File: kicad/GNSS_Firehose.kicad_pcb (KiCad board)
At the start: 4 copper layers, 117.9 x 99.1 mm, 4 parts

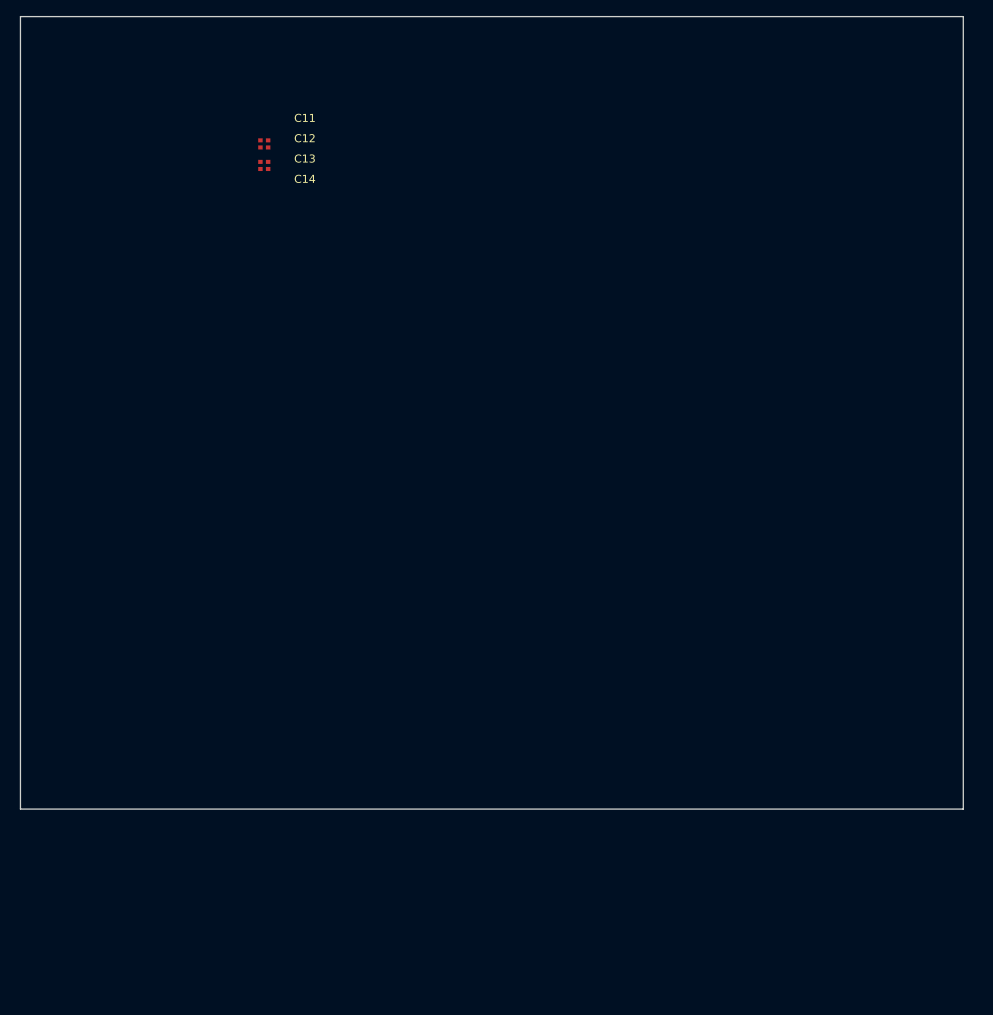
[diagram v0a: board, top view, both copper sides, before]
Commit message: footprints and footprint assignments
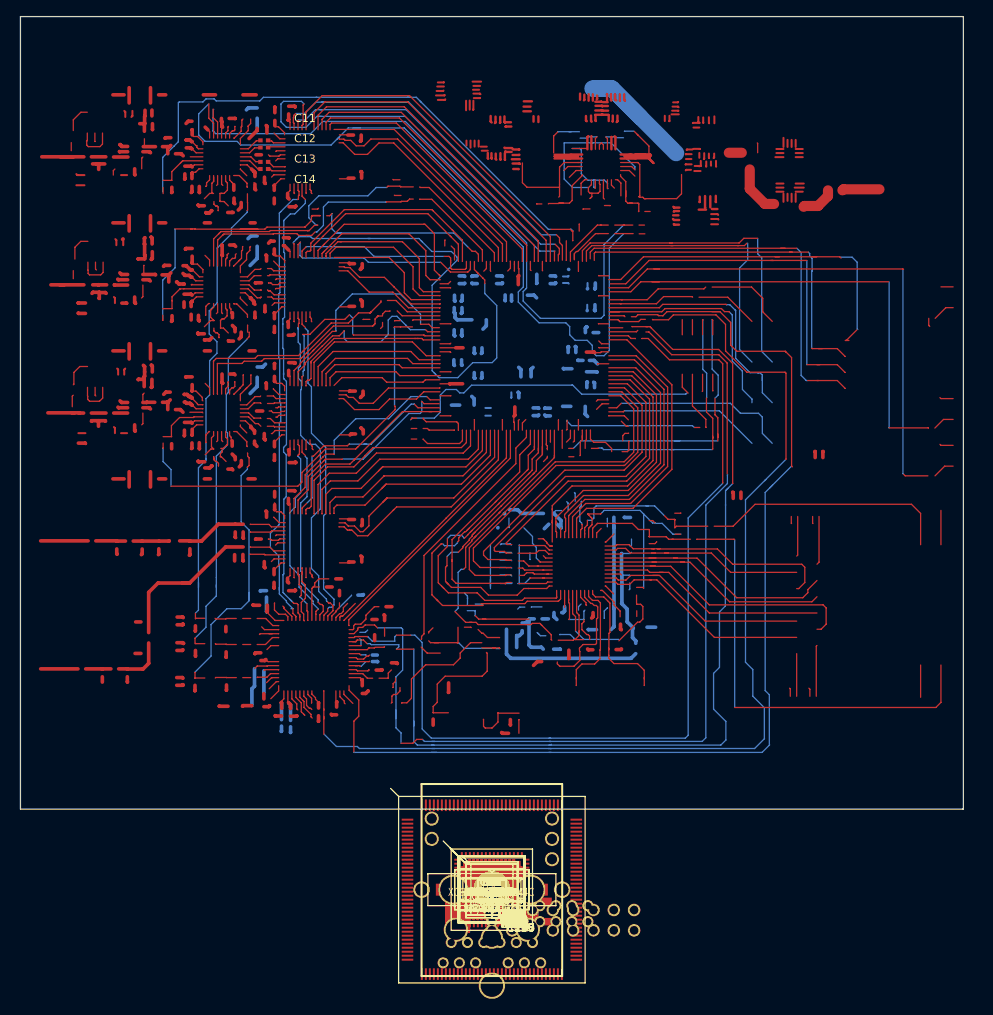
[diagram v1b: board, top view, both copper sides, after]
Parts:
- added C1, C10, C102, C108, C109, C110, C111, C112, C67, C73, C74, C75, C76, C77: 47 nF, footprints:0402, F.Cu at (132.6, 152.3)
- added C100, C116, C117, C126, C127, C128, C129, C130, C131, C132, C133, C134, C135, C137, C138, C139, C140, C141, C143, C144, C145, C146, C147, C149, C150, C151, C152, C153, C155, C156, C157, C159, C160, C161, C163, C164, C165, C167, C168, C18, C182, C183, C184, C185, C186, C187, C19, C201, C202, C203, C204, C205, C206, C207, C208, C209, C210, C211, C212, C218, C219, C221, C222, C223, C224, C227, C228, C229, C230, C248, C249, C250, C251, C252, C253, C254, C28, C29, C30, C31, C32, C33, C34, C35, C36, C37, C41, C42, C43, C44, C45, C46, C47, C49, C51, C54, C55, C56, C57, C58, C59, C60, C61, C62, C63, C64, C65, C66, C81, C82, C91, C92, C93, C94, C95, C96, C97, C98, C99: 0.1 uF, footprints:0402, F.Cu at (132.6, 152.3)
- added C103, C5, C68: 10 nF, footprints:0402, F.Cu at (132.6, 152.3)
- added C104, C105, C106, C107, C115, C125, C17, C27, C6, C69, C7, C70, C71, C72, C8, C80, C9, C90: 100 pF, footprints:0402, F.Cu at (132.6, 152.3)
- added C113, C15, C78: 2.2 nF, footprints:0402, F.Cu at (132.6, 152.3)
- added C114, C16, C79: 33 nF, footprints:0402, F.Cu at (132.6, 152.3)
- added C118, C119, C120, C121, C122, C123, C124, C20, C21, C22, C23, C24, C242, C243, C244, C245, C246, C247, C25, C26, C83, C84, C85, C86, C87, C88, C89: 1000 pF, footprints:0402, F.Cu at (132.6, 152.3)
- added C142, C148, C154, C158, C162, C166, C193, C216, C217, C220, C225, C226, C53: 10 uF, footprints:0805, F.Cu at (132.6, 152.3)
- added C176, C177: 33 pF, footprints:0402, F.Cu at (132.6, 152.3)
- added C194, C198: 47 uF 20V, footprints:tantalum-size-D, F.Cu at (132.6, 152.3)
- added C195: 2.2 uF, footprints:0603, F.Cu at (132.6, 152.3)
- added C196: 47 uF, footprints:1210, F.Cu at (132.6, 152.3)
- added C197, C199: 0.1 uF 25V, footprints:0402, F.Cu at (132.6, 152.3)
- added C200: 22 uF, footprints:1210, F.Cu at (132.6, 152.3)
- added C213, C237: NONE, footprints:1210, F.Cu at (132.6, 152.3)
- added C214: 220 pF, footprints:0402, F.Cu at (132.6, 152.3)
- added C215: 18 nF, footprints:0603, F.Cu at (132.6, 152.3)
- added C231, C232, C233, C234, C235, C236, C255: 10 pF, footprints:0402, F.Cu at (132.6, 152.3)
- added C238, C239, C240, C241, R108, R111, R112, R114, R115, R120, R121, R122, R125, R129, R130: NONE, footprints:0402, F.Cu at (132.6, 152.3)
- added FB1, FB11, FB12, FB13, FB14, FB15, FB16, FB2, FB3: 240, footprints:0603, F.Cu at (132.6, 152.3)
- added FB10, FB17, FB4, FB5, FB6, FB7, FB8, FB9: 240, footprints:0402, F.Cu at (132.6, 152.3)
- added FID1, FID2, FID3: fiducial, footprints:FIDUCIAL, F.Cu at (132.6, 152.3)
- added J1, J2, J3, J4, J5: SMA, footprints:SMA_END_LAUNCH, F.Cu at (132.6, 152.3)
- added J10: HEADER_16, footprints:HEADER16_100MIL, F.Cu at (132.6, 152.3)
- added J6: HEADER_14, footprints:HEADER14_2MM, F.Cu at (132.6, 152.3)
- added J7: L829-1J1T-43, footprints:L829-1J1T-43, F.Cu at (132.6, 152.3)
- added J8: PJ-063BH, footprints:PJ-063BH, F.Cu at (132.6, 152.3)
- added L10: 0.47 uF, footprints:NRS5020, F.Cu at (132.6, 152.3)
- added L11: 1 uH, footprints:NRS5020, F.Cu at (132.6, 152.3)
- added L12, L13, L14, L3, L5, L7: 47 nH, footprints:0402, F.Cu at (132.6, 152.3)
- added L15, L17, L19: 56 nH, footprints:0603, F.Cu at (132.6, 152.3)
- added L2, L4, L6: 6 nH, footprints:0402, F.Cu at (132.6, 152.3)
- added L20, L21, R126, R127, R128, R132, R98, R99: 0, footprints:0603, F.Cu at (132.6, 152.3)
- added LED1: LED, footprints:0603, F.Cu at (132.6, 152.3)
- added LED2, LED3, LED4: LED, footprints:APA2106, F.Cu at (132.6, 152.3)
- added MH1, MH2, MH3, MH4: mounting_hole, footprints:HOLE_UNC_2_56, F.Cu at (132.6, 152.3)
- added OSC1: TCXO, footprints:D75J, F.Cu at (132.6, 152.3)
- added Q1: Si2369DS, footprints:SOT23, F.Cu at (132.6, 152.3)
- added R1, R17, R25: 86.6, footprints:0402, F.Cu at (132.6, 152.3)
- added R10, R51, R52: 220, footprints:0402, F.Cu at (132.6, 152.3)
- added R100, R101, R102, R103, R104, R105: 33, footprints:0402, F.Cu at (132.6, 152.3)
- added R106, R109, R110, R113, R118, R119, R123, R137, R138, R139, R140, R141, R142, R40, R41, R86: 1k, footprints:0402, F.Cu at (132.6, 152.3)
- added R107, R44, R47: 4.7k, footprints:0402, F.Cu at (132.6, 152.3)
- added R11, R13, R15, R23, R31, R7: 80, footprints:0402, F.Cu at (132.6, 152.3)
- added R116, R117, R124, R146, R147, R148, R149, R150, R22, R30, R46, R6, R72, R73, R76, R77, R78, R79, R80, R81, R82, R83, R84, R97: 10k, footprints:0402, F.Cu at (132.6, 152.3)
- added R131, R135, R136, R42: 0, footprints:0402, F.Cu at (132.6, 152.3)
- added R133: 10, footprints:0603, F.Cu at (132.6, 152.3)
- added R143, R87: 0, footprints:1210, F.Cu at (132.6, 152.3)
- added R144: 10, footprints:0402, F.Cu at (132.6, 152.3)
- added R145: 0, footprints:0805, F.Cu at (132.6, 152.3)
- added R18, R2, R26: 5.1k, footprints:0402, F.Cu at (132.6, 152.3)
- added R19, R27, R3: 43.2, footprints:0402, F.Cu at (132.6, 152.3)
- added R20, R28, R4, R88: 820, footprints:0402, F.Cu at (132.6, 152.3)
- added R21, R29, R5: 390, footprints:0402, F.Cu at (132.6, 152.3)
- added R33, R37: 49.9, footprints:0402, F.Cu at (132.6, 152.3)
- added R34, R35: 60.4, footprints:0402, F.Cu at (132.6, 152.3)
- added R36: 249, footprints:0402, F.Cu at (132.6, 152.3)
- added R38, R39, R43, R48: 47, footprints:0402, F.Cu at (132.6, 152.3)
- added R45, R49, R50, R75, R85: 330, footprints:0402, F.Cu at (132.6, 152.3)
- added R70: 54.9k, footprints:0402, F.Cu at (132.6, 152.3)
- added R71: 12.1k, footprints:0402, F.Cu at (132.6, 152.3)
- added R74: 162k, footprints:0402, F.Cu at (132.6, 152.3)
- added R9: 150, footprints:0402, F.Cu at (132.6, 152.3)
- added R95: 12.1k 1%, footprints:0402, F.Cu at (132.6, 152.3)
- added R96: 470, footprints:0402, F.Cu at (132.6, 152.3)
- added SC1, SC2, SC3, SC4, SC5, SC6, SC7, SC8: shield_clip, footprints:S1721, F.Cu at (132.6, 152.3)
- added TP1, TP10, TP11, TP12, TP13, TP14, TP15, TP16, TP17, TP18, TP19, TP2, TP20, TP22, TP23, TP24, TP25, TP26, TP27, TP28, TP29, TP3, TP4, TP5, TP6, TP7, TP8, TP9: test_point, footprints:TP_SMT, F.Cu at (132.6, 152.3)
- added U1, U4, U7: MAX2112, footprints:QFN28_EP, F.Cu at (132.6, 152.3)
- added U10, U2, U5, U8: MAX19505, footprints:QFN48_EP, F.Cu at (132.6, 152.3)
- added U11: AT25DF041A, footprints:SO8, F.Cu at (132.6, 152.3)
- added U12: XC6SLX9-2TQG144C, footprints:LQFP144, F.Cu at (132.6, 152.3)
- added U15: LMK03806, footprints:LLP64_EP, F.Cu at (132.6, 152.3)
- added U17: LTC3633, footprints:UFD28, F.Cu at (132.6, 152.3)
- added U18: KSZ9031RNX, footprints:QFN48_EP_MICREL, F.Cu at (132.6, 152.3)
- added U19: CDCLVC1102, footprints:TSSOP8W, F.Cu at (132.6, 152.3)
- added U20, U21, U22: MIC2090-1YM5, footprints:SOT-23-5, F.Cu at (132.6, 152.3)
- added U3, U6, U9: MGA-68563, footprints:SOT-363, F.Cu at (132.6, 152.3)
- added Y1: 25 MHz, footprints:CTS_ATS, F.Cu at (132.6, 152.3)
- added Z1: SMAJ9.0CA, footprints:SMAJ, F.Cu at (132.6, 152.3)
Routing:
- net (no net): track 0.00 -> 6403.4 mm
- net Net-(C11-Pad1): track 0.00 -> 3.02 mm
- net Net-(C14-Pad1): track 0.00 -> 3.02 mm
- net Net-(C12-Pad1): track 0.00 -> 2.86 mm
- net Net-(C13-Pad1): track 0.00 -> 2.86 mm
- net Net-(C13-Pad2): track 0.00 -> 2.66 mm
- net Net-(C11-Pad2): track 0.00 -> 2.31 mm
- net Net-(C14-Pad2): track 0.00 -> 2.29 mm
- net Net-(C12-Pad2): track 0.00 -> 2.24 mm

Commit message: initial placement and wires
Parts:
- C141, C142, C143, C144, C145, C146, C147, C148, C149, C150, C151, C152, C153, C154, C155, C156, C157, C158, C159, C160, C161, C162, C163, C164, C165, C166, C167, C168, C182, C183, C184, C185, C186, C187, C193, C197, C199, C216, C217, C218, C219, C222, C223, C224, C225, C226, C227, C228, C59, C63, C65, FB1, FB11, FB12, FB13, FB3, FB4, FB5, FB7, FB9, R106, R107, R112, R113, R114, R115, R116, R117, R118, R119, R120, R121, R122, R123, R98, R99: moved to B.Cu
- moved FID3 117.2 mm to (76.2, 49.5)
- moved MH1 112.9 mm to (81.9, 51.4)
- moved MH2 112.9 mm to (183.3, 51.4)
- moved J1 109.1 mm to (73.2, 60.8), turned to 90 degrees
- moved SC1 108.7 mm to (88.5, 53.0)
- moved R126 107.8 mm to (80.1, 58.2), turned to 90 degrees
- moved U20 107.3 mm to (82.0, 57.7)
- moved C243 106.7 mm to (87.1, 55.7)
- moved J8 106.3 mm to (192.9, 64.8), turned to 270 degrees
- moved L12 106.1 mm to (80.0, 60.2), turned to 270 degrees
- moved C5 105.8 mm to (89.7, 55.6)
- moved C7 104.9 mm to (89.7, 56.6)
- moved C6 104.6 mm to (82.0, 60.7)
- moved SC2 104.6 mm to (99.8, 53.0)
- moved L3 103.9 mm to (89.2, 58.0), turned to 270 degrees
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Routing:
- net (no net): track 6403.4 -> 2297.0 mm
- net GND: track 0.00 -> 357.5 mm, vias 0 -> 1
- net VCC_3.3V: track 0.00 -> 235.2 mm
- net /Ethernet/DVDDL: track 0.00 -> 50.6 mm
- net PHY_RXD3: track 0.00 -> 46.7 mm
- net CH1_CLK: track 0.00 -> 44.0 mm
- net PHY_RX_CTL: track 0.00 -> 43.0 mm
- net PHY_RXD0: track 0.00 -> 42.3 mm
- net CH1_D7: track 0.00 -> 41.5 mm
- net PHY_RXD1: track 0.00 -> 40.1 mm
- net CH1_D6: track 0.00 -> 39.3 mm
- net VCC_1.2V: track 0.00 -> 38.7 mm
- net PHY_RXD2: track 0.00 -> 38.6 mm
- net CH1_D5: track 0.00 -> 37.1 mm
- net Net-(TP22-Pad1): track 0.00 -> 36.7 mm
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- added copper zone on In1.Cu, net GND
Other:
- net class Default: clearance 0.2 -> 0.1524; trace_width 0.25 -> 0.1524; via_dia 0.6 -> 0.6096; via_drill 0.4 -> 0.3048
- net class wide added: clearance 0.1524, trace_width 0.4572, via_dia 0.6096, via_drill 0.3048
- rule pad_to_mask_clearance: 0.2 -> 0
- rule trace_clearance: 0.2 -> 0.1524
- rule trace_min: 0.2 -> 0.1524
- rule via_min_drill: 0.3 -> 0.3048
- rule via_min_size: 0.4 -> 0.6096

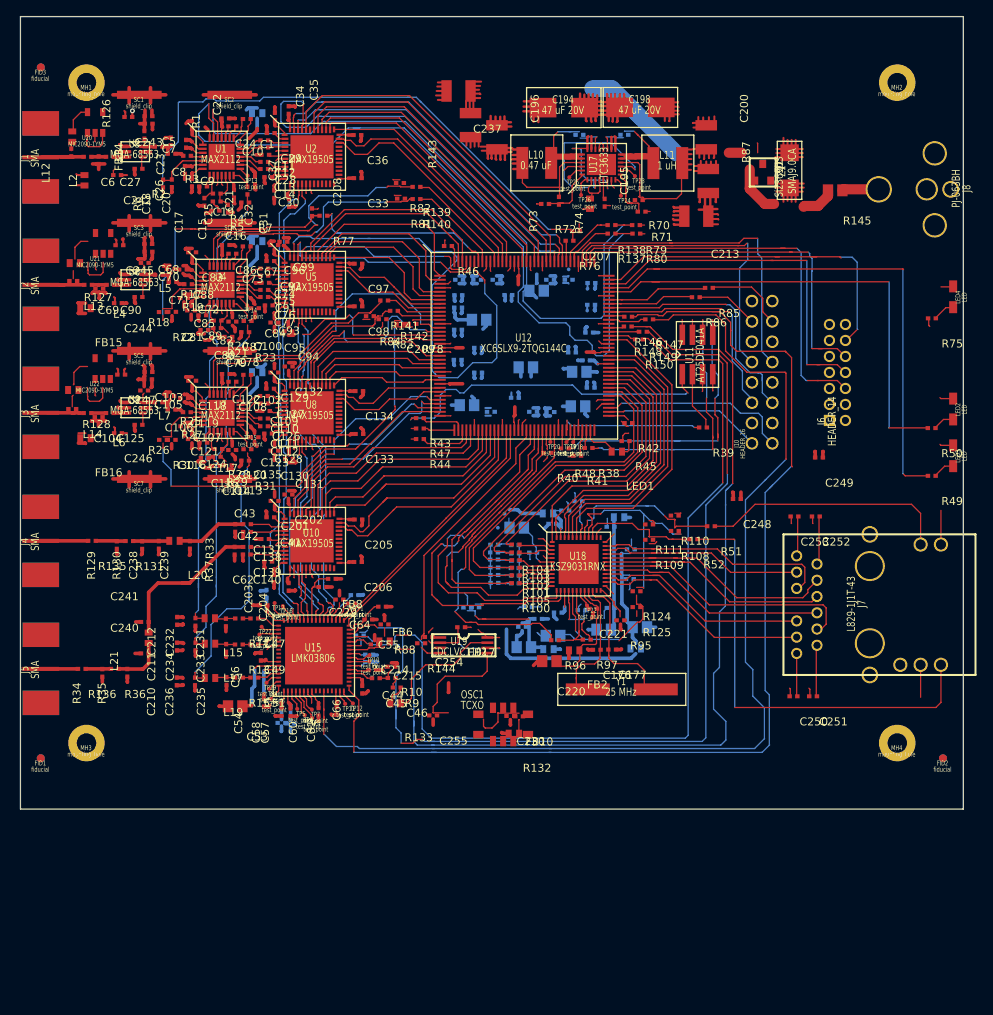
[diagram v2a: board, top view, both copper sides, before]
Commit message: fix component rotations and wire endpoints
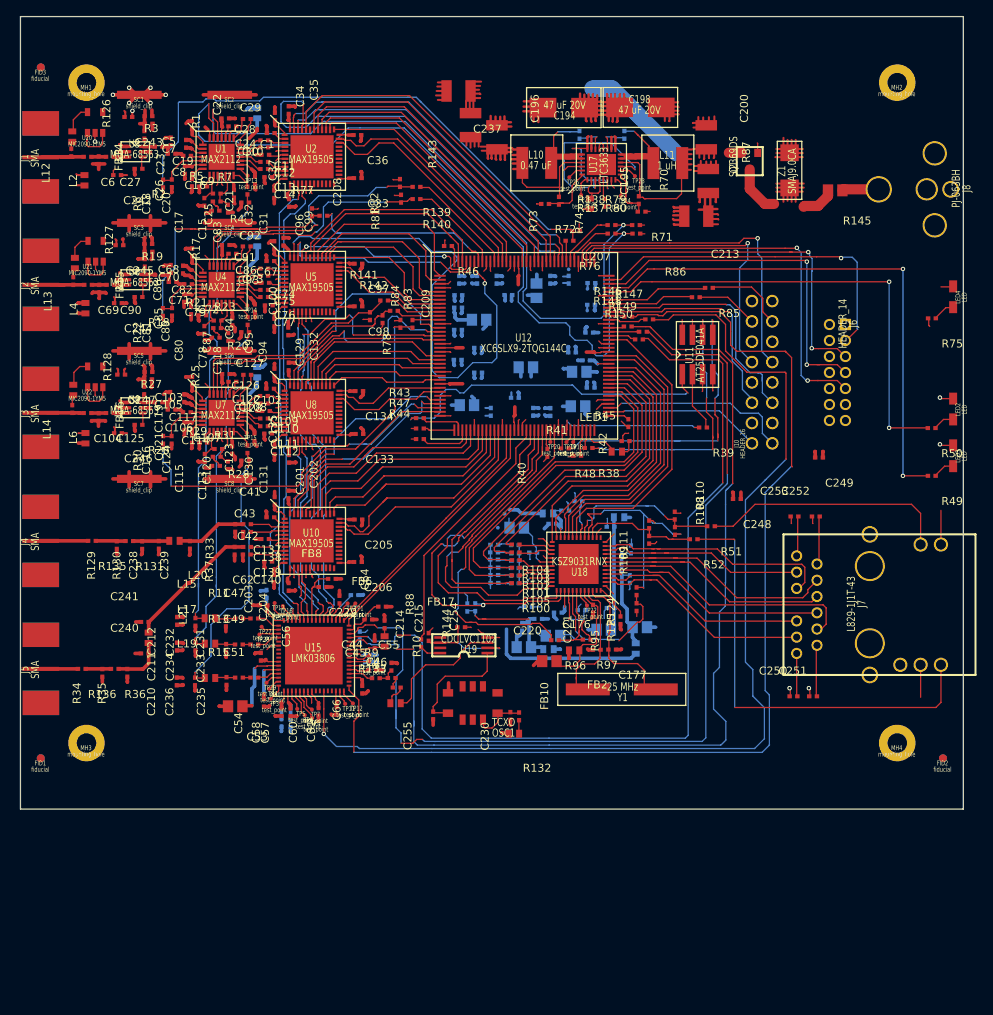
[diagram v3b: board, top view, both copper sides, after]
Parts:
- moved J6 13.4 mm to (178.8, 81.7), turned to 270 degrees
- moved OSC1 4.63 mm to (133.9, 131.7), turned to 180 degrees
- moved Q1 2.68 mm to (166.4, 63.0), turned to 180 degrees
- moved U22 1.39 mm to (82.1, 89.5)
- moved U21 1.35 mm to (82.1, 73.8)
- turned C100 to 90 degrees
- turned C113 to 270 degrees
- turned C114 to 180 degrees
- turned C115 to 270 degrees
- turned C116 to 270 degrees
- turned C117 to 180 degrees
- turned C118 to 90 degrees
- turned C119 to 270 degrees
- turned C120 to 270 degrees
- turned C121 to 270 degrees
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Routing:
- net (no net): track 2297.0 -> 1474.9 mm
- net CLOCK_READBACK: track 6.18 -> 128.9 mm, vias 0 -> 1
- net CH1_SCL: track 10.6 -> 97.2 mm, vias 0 -> 1
- net CH1_SDA: track 5.54 -> 86.3 mm, vias 0 -> 1
- net VCC_3.3V: track 235.2 -> 161.5 mm
- net CH2_CS: track 3.49 -> 62.0 mm, vias 0 -> 1
- net /FPGA/led0: track 10.4 -> 66.7 mm, vias 0 -> 2
- net /FPGA/led1: track 11.8 -> 58.7 mm, vias 0 -> 2
- net PHY_MDINT: track 3.58 -> 44.4 mm, vias 0 -> 1
- net PHY_MDIO: track 2.58 -> 41.9 mm
- net CLOCK_FTEST_LD: track 9.21 -> 47.4 mm
- net PHY_TXD0: track 3.13 -> 37.7 mm
- net Net-(TP22-Pad1): track 36.7 -> 2.19 mm
- net PHY_MDC: track 4.51 -> 38.3 mm
- net PHY_TXD1: track 4.28 -> 36.0 mm
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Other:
- net class Default: via_dia 0.6096 -> 0.5588
- net class wide: via_dia 0.6096 -> 0.5588
- rule pad_to_mask_clearance: 0 -> 0.0635
- rule via_min_size: 0.6096 -> 0.5588

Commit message: footprint and DRC fixes
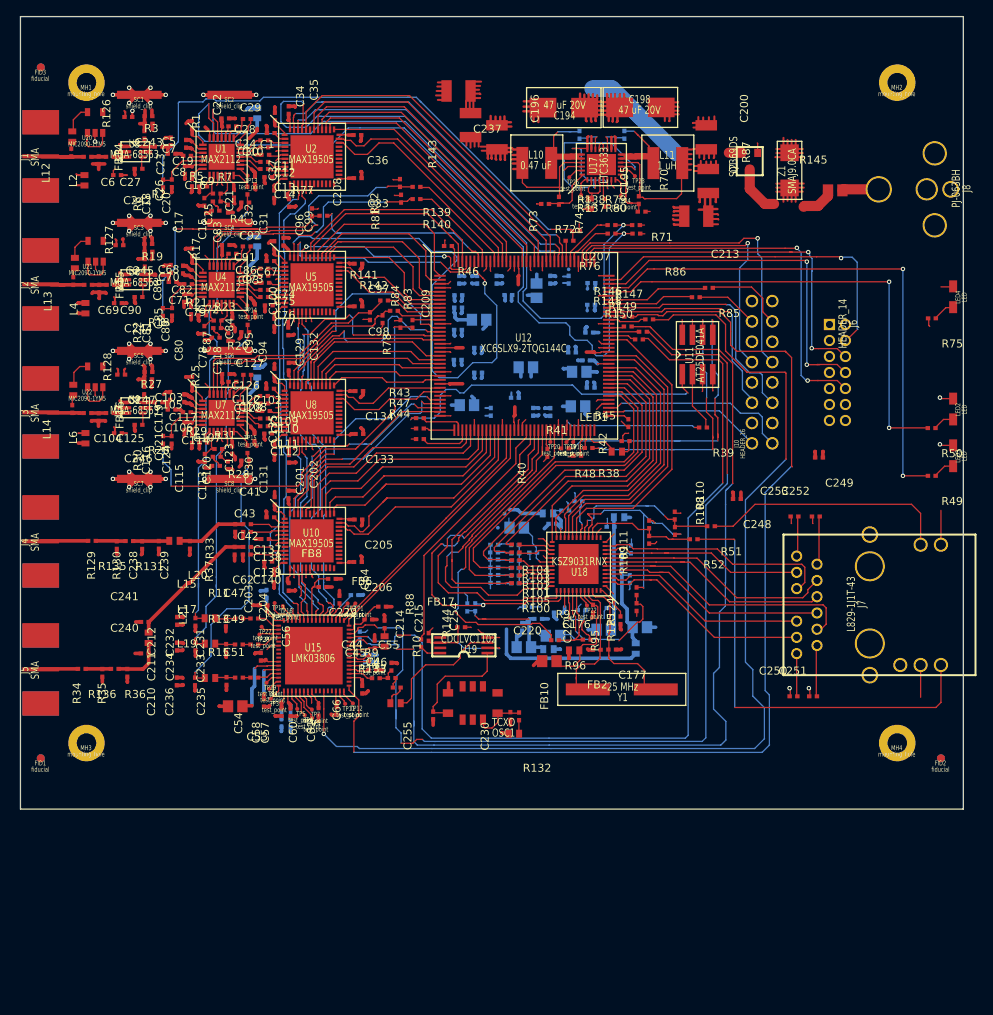
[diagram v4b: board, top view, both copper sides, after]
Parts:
- moved FID2 0.25 mm to (188.7, 135.9)
- moved J1 0.13 mm to (73.2, 60.6)
- moved J2 0.06 mm to (73.2, 76.6)
- moved J5 0.06 mm to (73.2, 124.8)
- moved J3 0.06 mm to (73.2, 92.6)
- moved J4 0.06 mm to (73.2, 108.8)
- turned C184 to 180 degrees
- turned C219 to 270 degrees
- turned C222 to 270 degrees
- turned C225 to 180 degrees
- turned C226 to 180 degrees
- turned C227 to 180 degrees
- turned C228 to 180 degrees
- turned FB3 to 180 degrees
- turned R112 to 180 degrees
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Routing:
- net (no net): track 1474.9 -> 1393.3 mm
- net GND: track 374.0 -> 430.9 mm, vias 12 -> 38
- net CH2_GC1_FPGA_LPF: track 12.7 -> 34.1 mm, vias 0 -> 2
- net /FPGA/spare2_p: track 18.7 -> 30.6 mm
- net PHY_NRESET: track 24.9 -> 36.5 mm
- net /Ethernet/AVDDH: track 7.44 -> 17.5 mm
- net /Ethernet/AVDDL: track 9.49 -> 18.6 mm
- net /Ethernet/DVDDH: track 25.0 -> 33.7 mm
- net PHY_RXD3: track 46.7 -> 38.1 mm
- net CLOCK_READBACK: track 128.9 -> 132.4 mm
- net Net-(J7-Pad3): track 25.7 -> 29.2 mm
- net Net-(J7-Pad2): track 27.4 -> 29.7 mm
- net /Ethernet/phyad0: track 7.32 -> 9.13 mm
- net Net-(J7-Pad8): track 24.1 -> 25.8 mm
- net PHY_RXD1: track 40.1 -> 41.7 mm
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- added copper zone on In1.Cu, net /Ethernet/chassis_gnd
- added copper zone on In2.Cu, net VCC_3.3V
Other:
- net class Default: clearance 0.1524 -> 0.15
- net class wide: clearance 0.1524 -> 0.15
- rule trace_clearance: 0.1524 -> 0.15
